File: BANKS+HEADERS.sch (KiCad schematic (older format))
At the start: 11 parts, among them J401 CONN_02X35, J402 CONN_02X35, U301 iCE40-HX4K-TQ144

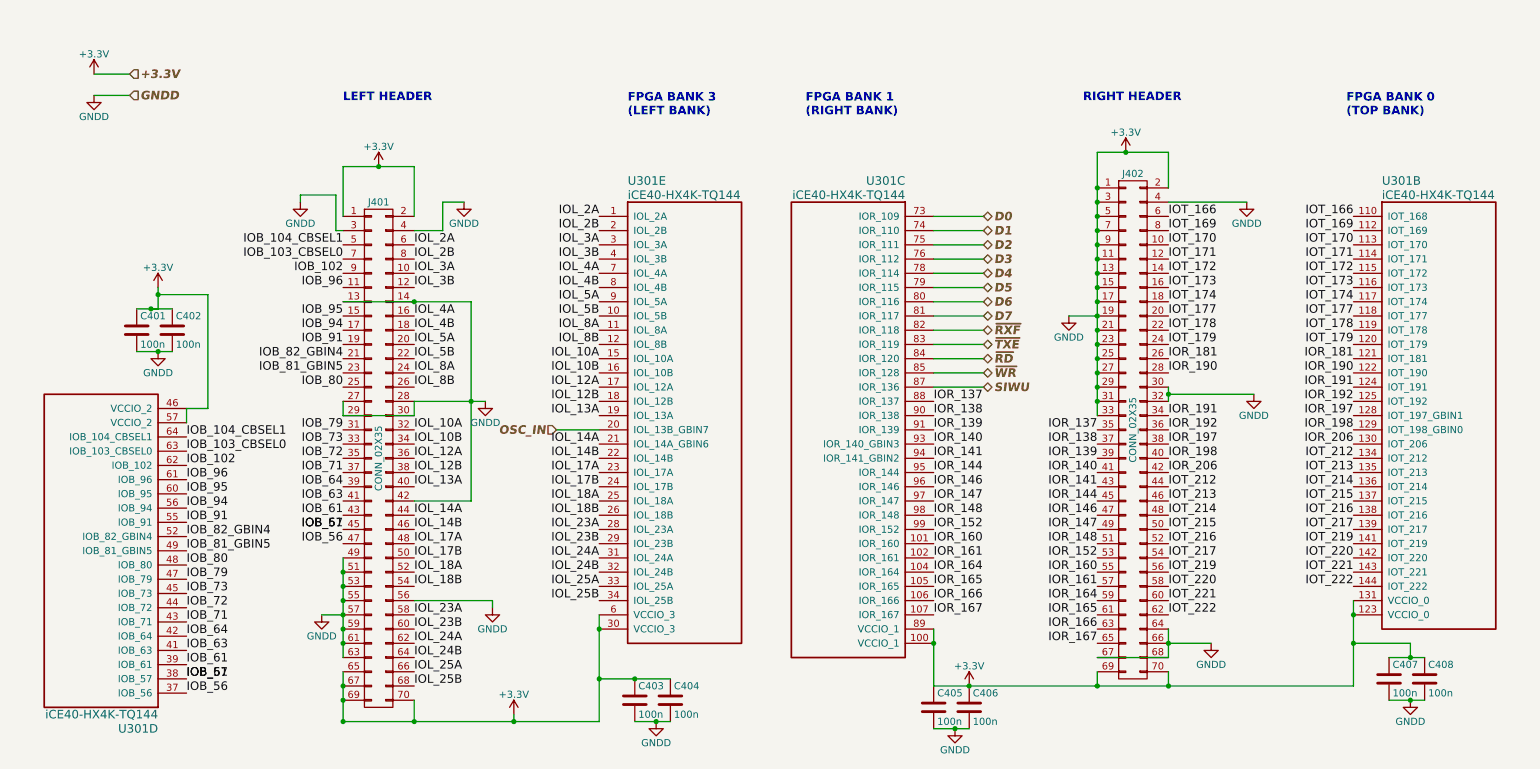
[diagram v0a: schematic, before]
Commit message: Reordered IO connections to FPGA
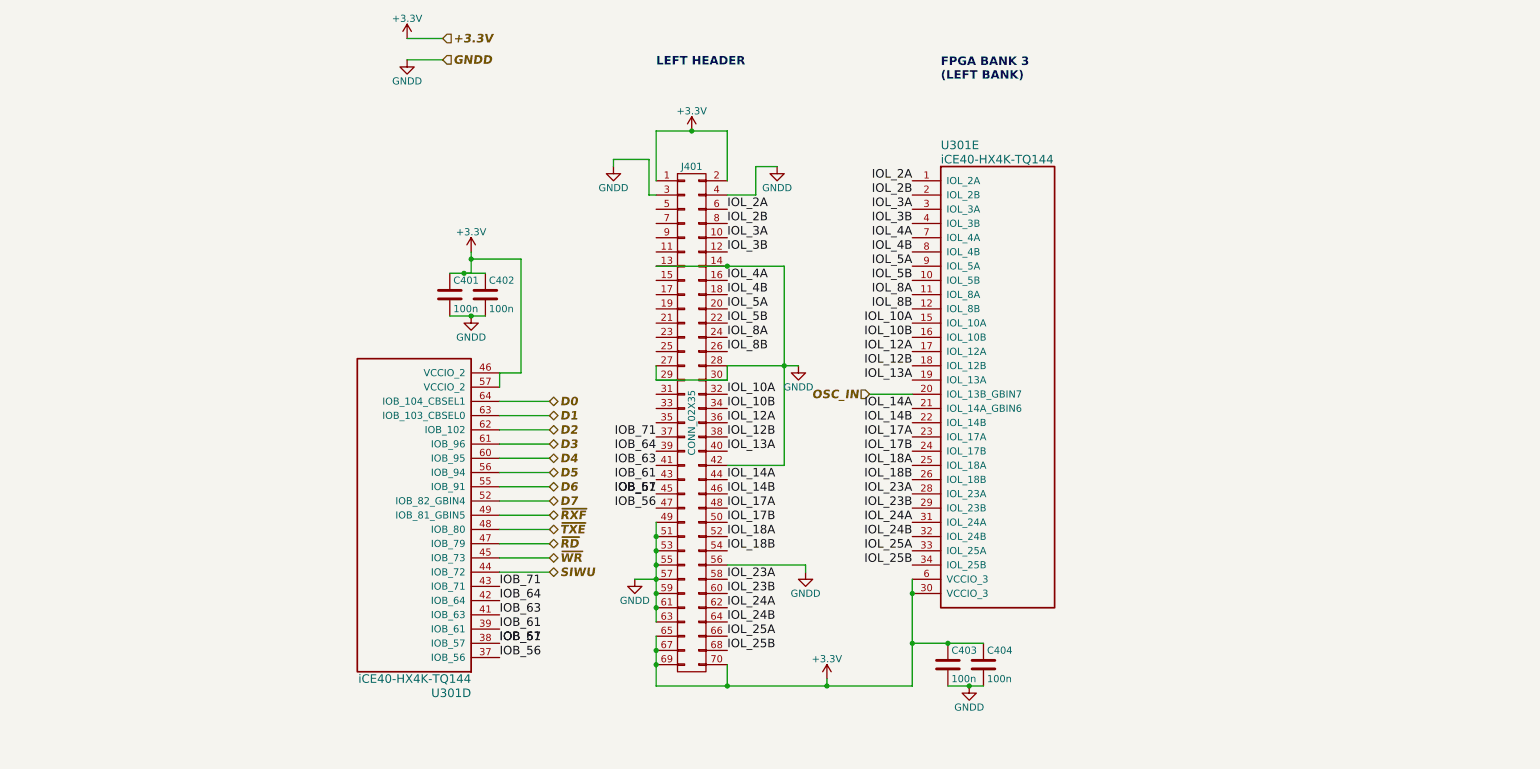
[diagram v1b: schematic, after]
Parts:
- removed C405, C406, C407, C408: 100n, symbol C
- removed J402: CONN_02X35, symbol CONN_02X35
- removed unit 2 of U301
- removed unit 3 of U301
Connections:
- net +3V3: no longer C401.2, C402.2, C403.2, C404.2, J401.13 (P13), J401.14 (P14), J401.27 (P27), J401.28 (P28), J401.29 (P29), J401.3 (P3), J401.30 (P30), J401.4 (P4), J401.42 (P42), J401.49 (P49), J401.51 (P51), J401.53 (P53), J401.55 (P55), J401.56 (P56), J401.57 (P57), J401.59 (P59), J401.61 (P61), J401.63 (P63)
- net D0: now also U301.64 (IOB_104_CBSEL1)
- net D1: now also U301.63 (IOB_103_CBSEL0)
- net D2: now also U301.62 (IOB_102)
- net D3: now also U301.61 (IOB_96)
- net D4: now also U301.60 (IOB_95)
- net D5: now also U301.56 (IOB_94)
- net D6: now also U301.55 (IOB_91)
- net D7: now also U301.52 (IOB_82_GBIN4)
- net SIWU: now also U301.44 (IOB_72)
- net ~RD: now also U301.47 (IOB_79)
- net ~RXF: now also U301.49 (IOB_81_GBIN5)
- net ~TXE: now also U301.48 (IOB_80)
- net ~WR: now also U301.45 (IOB_73)
- net IOB_102: no longer names the net of J401.9 (P9)
- net IOB_102: no longer U301.62 (IOB_102)
- net IOB_103_CBSEL0: no longer names the net of J401.7 (P7)
- net IOB_103_CBSEL0: no longer U301.63 (IOB_103_CBSEL0)
- net IOB_104_CBSEL1: no longer names the net of J401.5 (P5)
- net IOB_104_CBSEL1: no longer U301.64 (IOB_104_CBSEL1)
- net IOB_72: no longer names the net of J401.35 (P35)
- net IOB_72: no longer U301.44 (IOB_72)
- net IOB_73: no longer names the net of J401.33 (P33)
- net IOB_73: no longer U301.45 (IOB_73)
- net IOB_79: no longer names the net of J401.31 (P31)
- net IOB_79: no longer U301.47 (IOB_79)
- net IOB_80: no longer names the net of J401.25 (P25)
- net IOB_80: no longer U301.48 (IOB_80)
- net IOB_81_GBIN5: no longer names the net of J401.23 (P23)
- net IOB_81_GBIN5: no longer U301.49 (IOB_81_GBIN5)
- net IOB_82_GBIN4: no longer names the net of J401.21 (P21)
- net IOB_82_GBIN4: no longer U301.52 (IOB_82_GBIN4)
- net IOB_91: no longer names the net of J401.19 (P19)
- net IOB_91: no longer U301.55 (IOB_91)
- net IOB_94: no longer names the net of J401.17 (P17)
- net IOB_94: no longer U301.56 (IOB_94)
- net IOB_95: no longer names the net of J401.15 (P15)
- net IOB_95: no longer U301.60 (IOB_95)
- net IOB_96: no longer names the net of J401.11 (P11)
- net IOB_96: no longer U301.61 (IOB_96)
- new net GNDD: C401.2, C402.2, C403.2, C404.2, J401.13 (P13), J401.14 (P14), J401.27 (P27), J401.28 (P28), J401.29 (P29), J401.3 (P3), J401.30 (P30), J401.4 (P4), J401.42 (P42), J401.49 (P49), J401.51 (P51), J401.53 (P53), J401.55 (P55), J401.56 (P56), J401.57 (P57), J401.59 (P59), J401.61 (P61), J401.63 (P63)
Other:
- note removed: "FPGA BANK 0\n(TOP BANK)"
- note removed: "FPGA BANK 1\n(RIGHT BANK)"
- note removed: "RIGHT HEADER"
- moved on the sheet: C401, C402, C403, C404, J401, U301D, U301E

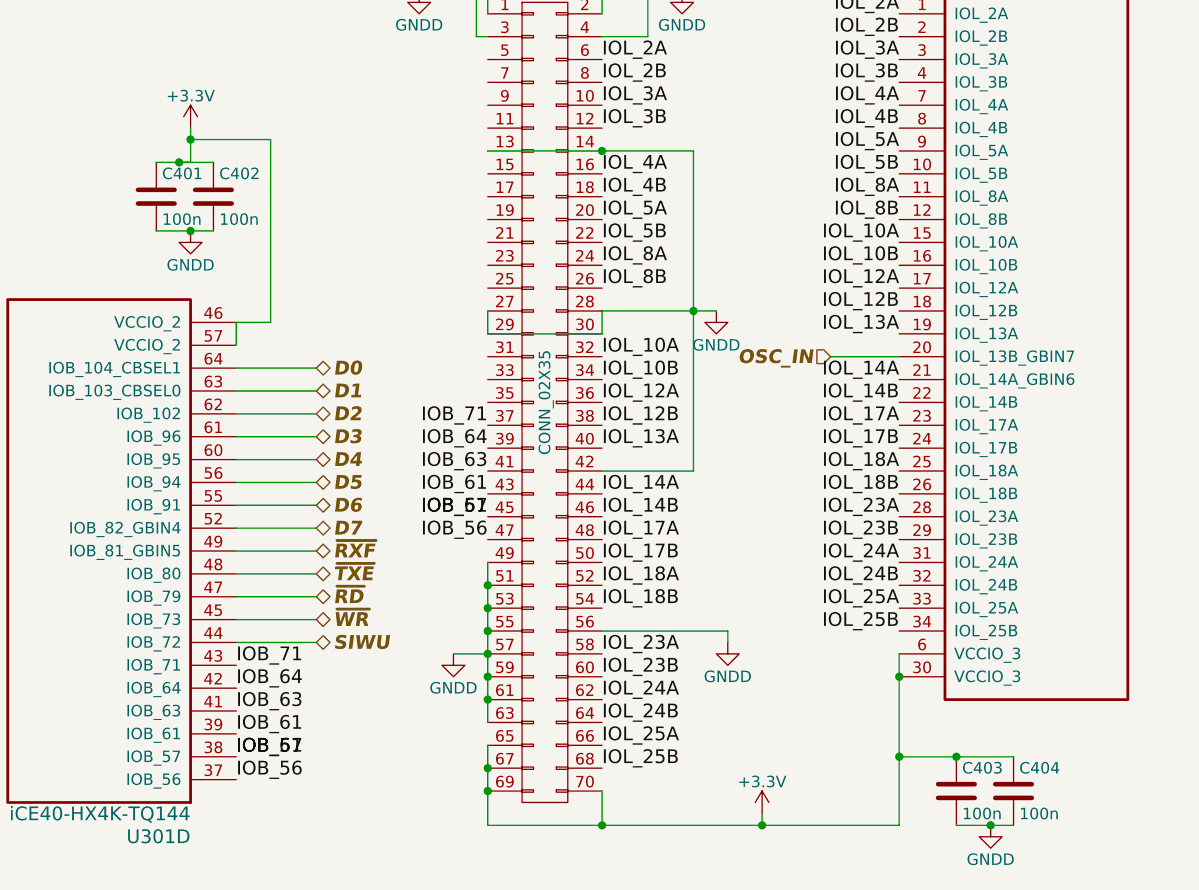
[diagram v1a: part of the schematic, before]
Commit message: Added part number and specifications on all sheets
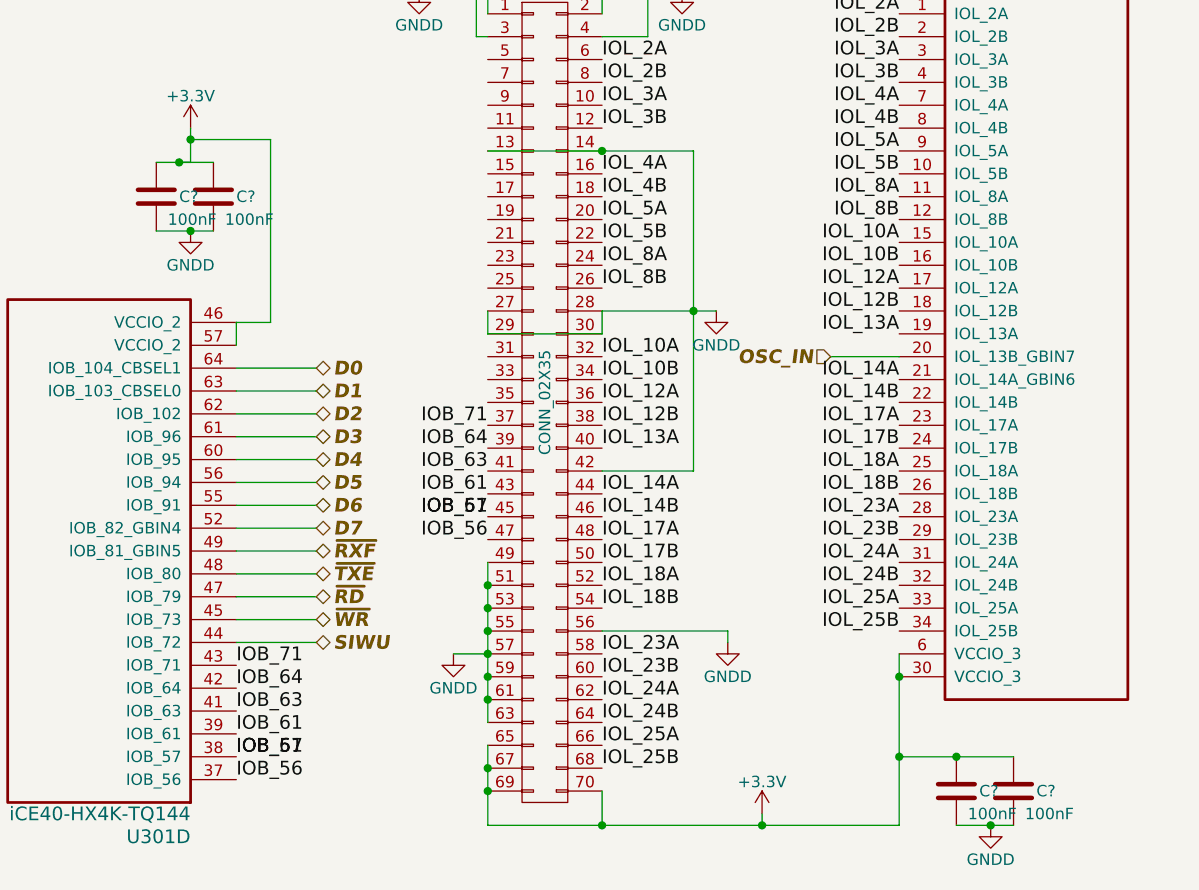
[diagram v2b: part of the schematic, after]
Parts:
- removed C401, C402, C403, C404: 100n, symbol C
- added C? (x4): 100nF, Capacitors_SMD:C_0603_HandSoldering, symbol C
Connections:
- net +3V3: now also C?.1, C?.1, C?.1, C?.1
- net GNDD: now also C?.2, C?.2, C?.2, C?.2
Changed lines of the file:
@@
-$EndComp
-$Comp
-L C C403
-U 1 1 58DDBC5E
-P 7050 5350
-F 0 "C403" H 7075 5450 50  0000 L CNN
-F 1 "100n" H 7075 5250 50  0000 L CNN
-F 2 "" H 7088 5200 50  0001 C CNN
-F 3 "" H 7050 5350 50  0001 C CNN
-	1    7050 5350
-	1    0    0    -1
-$EndComp
-$Comp
-L C C404
-U 1 1 58DDBC9F
-P 7300 5350
-F 0 "C404" H 7325 5450 50  0000 L CNN
-F 1 "100n" H 7325 5250 50  0000 L CNN
-F 2 "" H 7338 5200 50  0001 C CNN
-F 3 "" H 7300 5350 50  0001 C CNN
-	1    7300 5350
-	1    0    0    -1
 $EndComp
 $Comp
@@
 $EndComp
 $Comp
-L C C401
-U 1 1 58DF75FD
-P 3550 2750
-F 0 "C401" H 3575 2850 50  0000 L CNN
-F 1 "100n" H 3575 2650 50  0000 L CNN
-F 2 "" H 3588 2600 50  0001 C CNN
-F 3 "" H 3550 2750 50  0001 C CNN
-	1    3550 2750
-	1    0    0    -1
-$EndComp
-$Comp
-L C C402
-U 1 1 58DF7603
-P 3800 2750
-F 0 "C402" H 3825 2850 50  0000 L CNN
-F 1 "100n" H 3825 2650 50  0000 L CNN
-F 2 "" H 3838 2600 50  0001 C CNN
-F 3 "" H 3800 2750 50  0001 C CNN
-	1    3800 2750
-	1    0    0    -1
-$EndComp
-$Comp
 L GNDD #PWR078
 U 1 1 58DF7609
@@
 	6200 5450 6200 5500
 Connection ~ 6200 5500
+$Comp
+L C C?
+U 1 1 58E8E924
+P 7300 5350
+F 0 "C?" H 7400 5350 50  0000 L CNN
+F 1 "100nF" H 7350 5250 50  0000 L CNN
+F 2 "Capacitors_SMD:C_0603_HandSoldering" H 7338 5200 50  0001 C CNN
+F 3 "http://www.mouser.com/ds/2/212/KEM_C1002_X7R_SMD-357932.pdf" H 7300 5350 50  0001 C CNN
+F 4 "C0603C104K3RACTU" H 7300 5350 60  0001 C CNN "Manufacturer Part"
+F 5 "X7R" H 7300 5350 60  0001 C CNN "Dielectric"
+F 6 "25V (min. 10V)" H 7300 5350 60  0001 C CNN "VDC"
+	1    7300 5350
+	1    0    0    -1
+$EndComp
+$Comp
+L C C?
+U 1 1 58E8E956
+P 3550 2750
+F 0 "C?" H 3650 2750 50  0000 L CNN
+F 1 "100nF" H 3600 2650 50  0000 L CNN
+F 2 "Capacitors_SMD:C_0603_HandSoldering" H 3588 2600 50  0001 C CNN
+F 3 "http://www.mouser.com/ds/2/212/KEM_C1002_X7R_SMD-357932.pdf" H 3550 2750 50  0001 C CNN
+F 4 "C0603C104K3RACTU" H 3550 2750 60  0001 C CNN "Manufacturer Part"
+F 5 "X7R" H 3550 2750 60  0001 C CNN "Dielectric"
+F 6 "25V (min. 10V)" H 3550 2750 60  0001 C CNN "VDC"
+	1    3550 2750
+	1    0    0    -1
+$EndComp
+$Comp
+L C C?
+U 1 1 58E8E993
+P 3800 2750
+F 0 "C?" H 3900 2750 50  0000 L CNN
+F 1 "100nF" H 3850 2650 50  0000 L CNN
+F 2 "Capacitors_SMD:C_0603_HandSoldering" H 3838 2600 50  0001 C CNN
+F 3 "http://www.mouser.com/ds/2/212/KEM_C1002_X7R_SMD-357932.pdf" H 3800 2750 50  0001 C CNN
+F 4 "C0603C104K3RACTU" H 3800 2750 60  0001 C CNN "Manufacturer Part"
+F 5 "X7R" H 3800 2750 60  0001 C CNN "Dielectric"
+F 6 "25V (min. 10V)" H 3800 2750 60  0001 C CNN "VDC"
+	1    3800 2750
+	1    0    0    -1
+$EndComp
+$Comp
+L C C?
+U 1 1 58E8E9D1
+P 7050 5350
+F 0 "C?" H 7150 5350 50  0000 L CNN
+F 1 "100nF" H 7100 5250 50  0000 L CNN
+F 2 "Capacitors_SMD:C_0603_HandSoldering" H 7088 5200 50  0001 C CNN
+F 3 "http://www.mouser.com/ds/2/212/KEM_C1002_X7R_SMD-357932.pdf" H 7050 5350 50  0001 C CNN
+F 4 "C0603C104K3RACTU" H 7050 5350 60  0001 C CNN "Manufacturer Part"
+F 5 "X7R" H 7050 5350 60  0001 C CNN "Dielectric"
+F 6 "25V (min. 10V)" H 7050 5350 60  0001 C CNN "VDC"
+	1    7050 5350
+	1    0    0    -1
+$EndComp
 $EndSCHEMATC
